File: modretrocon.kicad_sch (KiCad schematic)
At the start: 0 parts

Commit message: Power rail stuff
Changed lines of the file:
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@@
 	(paper "A4")
 	(sheet
-		(at 63.5 63.5)
+		(at 101.6 50.8)
 		(size 12.7 3.81)
 		(exclude_from_sim no)
@@
 		)
 		(property "Sheetname" "IO"
-			(at 63.5 62.7884 0)
+			(at 101.6 50.0884 0)
 			(show_name no)
 			(do_not_autoplace no)
@@
 		)
 		(property "Sheetfile" "io.kicad_sch"
-			(at 63.5 67.8946 0)
+			(at 101.6 55.1946 0)
 			(show_name no)
 			(do_not_autoplace no)
@@
 	)
 	(sheet
-		(at 63.5 76.2)
+		(at 139.7 50.8)
 		(size 12.7 3.81)
 		(exclude_from_sim no)
@@
 		)
 		(property "Sheetname" "MCU"
-			(at 63.5 75.4884 0)
+			(at 139.7 50.0884 0)
 			(show_name no)
 			(do_not_autoplace no)
@@
 		)
 		(property "Sheetfile" "mcu.kicad_sch"
-			(at 63.5 80.5946 0)
+			(at 139.7 55.1946 0)
 			(show_name no)
 			(do_not_autoplace no)

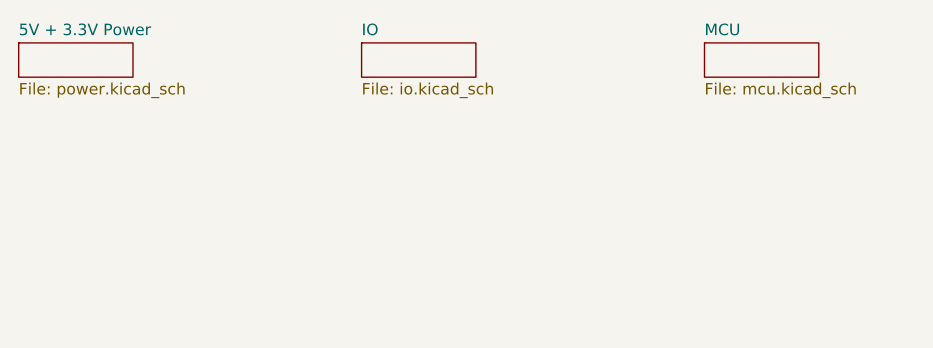
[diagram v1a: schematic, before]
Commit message: A lot re-wiring, added appropriate parts for schematic components. Some re-organization.
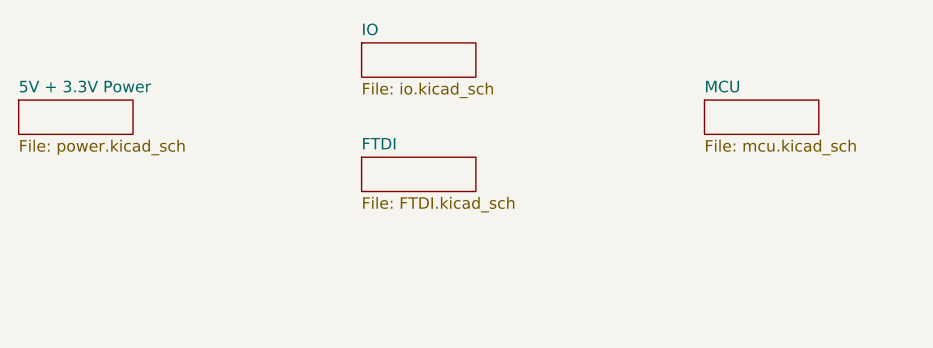
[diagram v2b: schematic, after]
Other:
- added sheet FTDI (FTDI.kicad_sch)
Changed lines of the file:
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@@
 	)
 	(sheet
-		(at 139.7 50.8)
+		(at 139.7 57.15)
 		(size 12.7 3.81)
 		(exclude_from_sim no)
@@
 		)
 		(property "Sheetname" "MCU"
-			(at 139.7 50.0884 0)
+			(at 139.7 56.4384 0)
 			(show_name no)
 			(do_not_autoplace no)
@@
 		)
 		(property "Sheetfile" "mcu.kicad_sch"
-			(at 139.7 55.1946 0)
+			(at 139.7 61.5446 0)
 			(show_name no)
 			(do_not_autoplace no)
@@
 	)
 	(sheet
-		(at 63.5 50.8)
+		(at 101.6 63.5)
+		(size 12.7 3.81)
+		(exclude_from_sim no)
+		(in_bom yes)
+		(on_board yes)
+		(dnp no)
+		(fields_autoplaced yes)
+		(stroke
+			(width 0.1524)
+			(type solid)
+		)
+		(fill
+			(color 0 0 0 0)
+		)
+		(property "Sheetname" "FTDI"
+			(at 101.6 62.7884 0)
+			(show_name no)
+			(do_not_autoplace no)
+			(effects
+				(font
+					(size 1.27 1.27)
+				)
+				(justify left bottom)
+			)
+		)
+		(property "Sheetfile" "FTDI.kicad_sch"
+			(at 101.6 67.8946 0)
+			(show_name no)
+			(do_not_autoplace no)
+			(effects
+				(font
+					(size 1.27 1.27)
+				)
+				(justify left top)
+			)
+		)
+		(instances
+			(project "modretrocon"
+				(path "/cf6749e4-132f-4e26-b0d6-92782ee54bed"
+					(page "5")
+				)
+			)
+		)
+	)
+	(sheet
+		(at 63.5 57.15)
 		(size 12.7 3.81)
 		(exclude_from_sim no)
@@
 		)
 		(property "Sheetname" "5V + 3.3V Power"
-			(at 63.5 50.0884 0)
+			(at 63.5 56.4384 0)
 			(show_name no)
 			(do_not_autoplace no)
@@
 		)
 		(property "Sheetfile" "power.kicad_sch"
-			(at 63.5 55.1946 0)
+			(at 63.5 61.5446 0)
 			(show_name no)
 			(do_not_autoplace no)
